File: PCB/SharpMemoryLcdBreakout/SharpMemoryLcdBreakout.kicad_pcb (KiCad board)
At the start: 2 copper layers, 14 x 42 mm, 8 parts, among them J1 Pin Header, J2 EMD, J5 FH12-10S-0.5SH

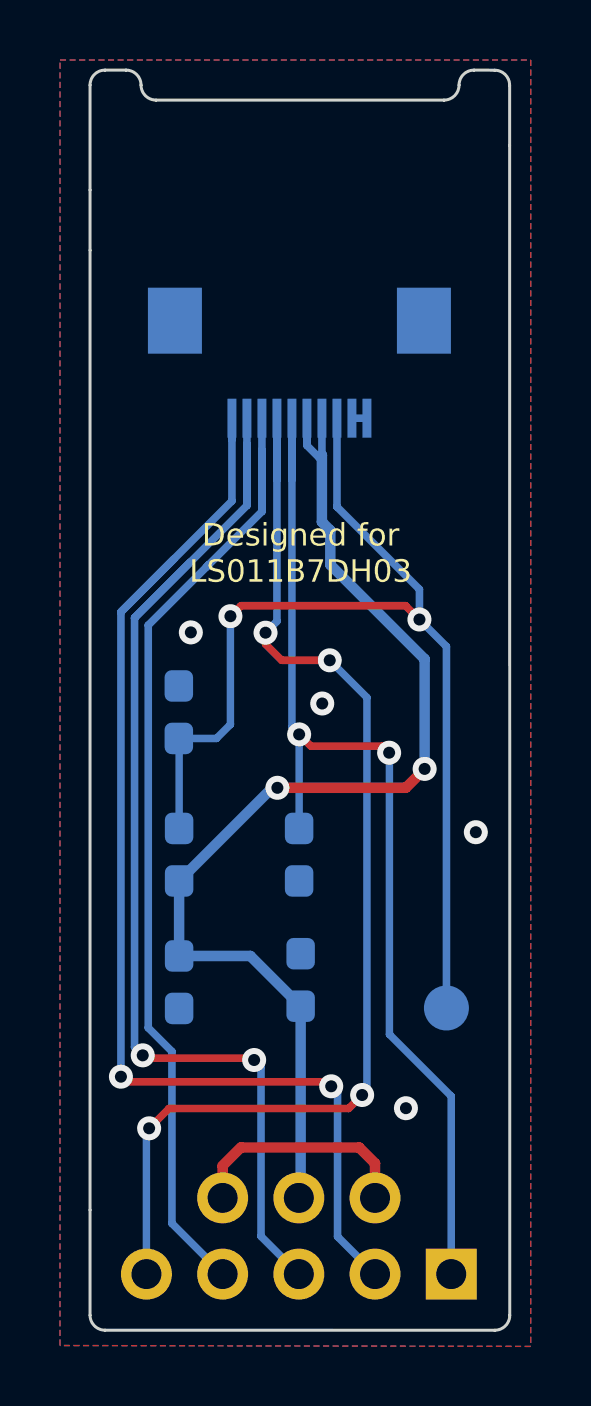
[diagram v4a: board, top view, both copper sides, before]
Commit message: increased part size (0805) and improved silk screen and added ferrite beads
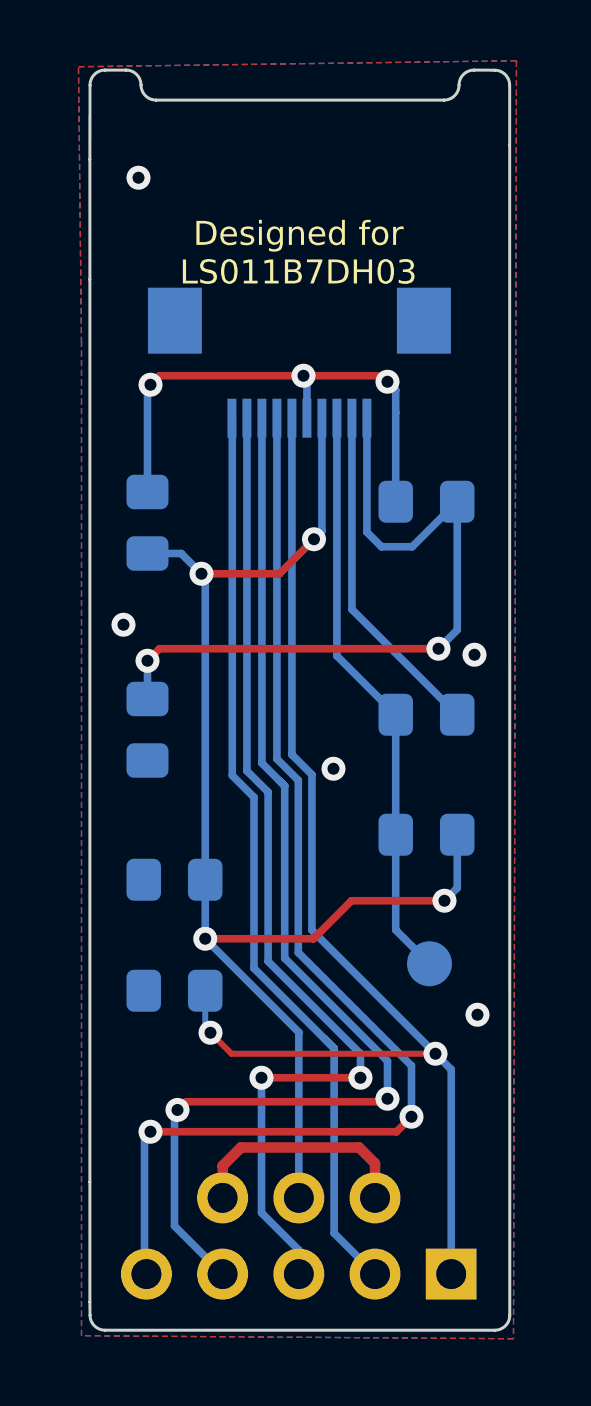
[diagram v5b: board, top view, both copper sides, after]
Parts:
- added FB1: Ferrite_Bead, Resistor_SMD:R_0805_2012Metric_Pad1.15x1.40mm_HandSolder, B.Cu at (104.5, 51.7)
- added FB2: Ferrite_Bead, Resistor_SMD:R_0805_2012Metric_Pad1.15x1.40mm_HandSolder, B.Cu at (104.5, 58.6)
- C1: footprint Capacitor_SMD:C_0603_1608Metric_Pad1.05x0.95mm_HandSolder -> Capacitor_SMD:C_0805_2012Metric_Pad1.15x1.40mm_HandSolder
- C2, C3: value 0.1uF -> 1uF; footprint Capacitor_SMD:C_0603_1608Metric_Pad1.05x0.95mm_HandSolder -> Capacitor_SMD:C_0805_2012Metric_Pad1.15x1.40mm_HandSolder
- R1, R2: footprint Resistor_SMD:R_0603_1608Metric_Pad1.05x0.95mm_HandSolder -> Resistor_SMD:R_0805_2012Metric_Pad1.15x1.40mm_HandSolder
- moved C2 16.5 mm to (113.8, 51.0), turned to 0 degrees
- moved R2 8.27 mm to (113.8, 62.1), turned to 180 degrees
- moved R1 8.26 mm to (113.8, 58.1), turned to 0 degrees
- moved C1 6.15 mm to (105.4, 67.3), turned to 180 degrees
- moved C3 3.42 mm to (105.4, 63.6), turned to 180 degrees
- moved J2 1.58 mm to (113.9, 66.4)
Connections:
- net Net-(C1-Pad1) renamed /DISP
- net Net-(J1-Pad2) renamed /SCLK
- net Net-(J1-Pad3) renamed /SI
- net Net-(J1-Pad4) renamed /SCS
- net Net-(J1-Pad5) renamed /EXTCOMIN
- net Net-(J2-Pad1) renamed /EXTMODE
- C2 pad 1: +3V3 -> VDDA
- C2 pad 2: GND -> GNDA
- J5 pad 10: GND -> GNDA
- J5 pad 6: +3V3 -> VDDA
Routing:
- net GNDA: track 0.00 -> 24.2 mm, vias 0 -> 2
- net VDDA: track 0.00 -> 17.3 mm, vias 0 -> 3
- net /EXTMODE: track 36.5 -> 19.5 mm, vias 2 -> 0
- net GND: track 8.27 -> 19.1 mm, vias 4 -> 5
- net /SCLK: track 40.7 -> 31.0 mm, vias 2 -> 0
- net /SI: track 39.1 -> 33.9 mm
- net +3V3: track 38.8 -> 43.5 mm, vias 2 -> 4
- net /SCS: track 33.3 -> 38.0 mm, vias 0 -> 2
- net /DISP: track 37.3 -> 40.0 mm
- net /EXTCOMIN: track 39.6 -> 39.0 mm, vias 4 -> 2
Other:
- outline, holes or cut-outs redrawn
- board text added: "Sharp Memory LCD Breakout v0.3"
- board text removed: "Sharp Memory LCD Breakout v0.2"

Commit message: Added BOM to readme and updated LCSC parts
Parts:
- C1: value 0.1uF -> 560pF
- renumbered J5 to J3
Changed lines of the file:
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@@
     (property "Sheetname" "")
     (attr smd)
-    (fp_text reference "J5" (at 0.04 -1.4) (layer "B.SilkS")
+    (fp_text reference "J3" (at 0.04 -1.4) (layer "B.SilkS")
       (effects (font (size 0.6 0.6) (thickness 0.1)) (justify mirror))
     )
@@
     (fp_line (start -4.05 1.2) (end -4.05 -3.4) (layer "B.Fab") (width 0.1))
     (pad "1" smd rect (at -2.25 1.85) (locked) (size 0.3 1.3) (layers "B.Cu" "B.Paste" "B.Mask")
-      (net 6 "/SCLK") (pinfunction "Pin_1"))
+      (net 6 "/SCLK") (pinfunction "Pin_1") (pintype "passive"))
     (pad "2" smd rect (at -1.75 1.85) (locked) (size 0.3 1.3) (layers "B.Cu" "B.Paste" "B.Mask")
-      (net 7 "/SI") (pinfunction "Pin_2"))
+      (net 7 "/SI") (pinfunction "Pin_2") (pintype "passive"))
     (pad "3" smd rect (at -1.25 1.85) (locked) (size 0.3 1.3) (layers "B.Cu" "B.Paste" "B.Mask")
-      (net 8 "/SCS") (pinfunction "Pin_3"))
+      (net 8 "/SCS") (pinfunction "Pin_3") (pintype "passive"))
     (pad "4" smd rect (at -0.75 1.85) (locked) (size 0.3 1.3) (layers "B.Cu" "B.Paste" "B.Mask")
-      (net 9 "/EXTCOMIN") (pinfunction "Pin_4"))
+      (net 9 "/EXTCOMIN") (pinfunction "Pin_4") (pintype "passive"))
     (pad "5" smd rect (at -0.25 1.85) (locked) (size 0.3 1.3) (layers "B.Cu" "B.Paste" "B.Mask")
-      (net 2 "/DISP") (pinfunction "Pin_5"))
+      (net 2 "/DISP") (pinfunction "Pin_5") (pintype "passive"))
     (pad "6" smd rect (at 0.25 1.85) (locked) (size 0.3 1.3) (layers "B.Cu" "B.Paste" "B.Mask")
-      (net 4 "VDDA") (pinfunction "Pin_6"))
+      (net 4 "VDDA") (pinfunction "Pin_6") (pintype "passive"))
     (pad "7" smd rect (at 0.75 1.85) (locked) (size 0.3 1.3) (layers "B.Cu" "B.Paste" "B.Mask")
-      (net 3 "+3V3") (pinfunction "Pin_7"))
+      (net 3 "+3V3") (pinfunction "Pin_7") (pintype "passive"))
     (pad "8" smd rect (at 1.25 1.85) (locked) (size 0.3 1.3) (layers "B.Cu" "B.Paste" "B.Mask")
-      (net 10 "/EXTMODE") (pinfunction "Pin_8"))
+      (net 10 "/EXTMODE") (pinfunction "Pin_8") (pintype "passive"))
     (pad "9" smd rect (at 1.75 1.85) (locked) (size 0.3 1.3) (layers "B.Cu" "B.Paste" "B.Mask")
-      (net 1 "GND") (pinfunction "Pin_9"))
+      (net 1 "GND") (pinfunction "Pin_9") (pintype "passive"))
     (pad "10" smd rect (at 2.25 1.85) (locked) (size 0.3 1.3) (layers "B.Cu" "B.Paste" "B.Mask")
-      (net 5 "GNDA") (pinfunction "Pin_10"))
+      (net 5 "GNDA") (pinfunction "Pin_10") (pintype "passive"))
     (pad "MP" smd rect (at 4.15 -1.4) (locked) (size 1.8 2.2) (layers "B.Cu" "B.Paste" "B.Mask"))
     (pad "MP" smd rect (at -4.15 -1.4) (locked) (size 1.8 2.2) (layers "B.Cu" "B.Paste" "B.Mask"))
@@
     (fp_circle (center 0 0) (end 1.25 0) (layer "B.CrtYd") (width 0.05) (fill none))
     (pad "1" smd circle (at 0 0 180) (locked) (size 1.5 1.5) (layers "B.Cu" "B.Mask")
-      (net 10 "/EXTMODE") (pinfunction "Pin_1"))
+      (net 10 "/EXTMODE") (pinfunction "Pin_1") (pintype "passive"))
   )
   (footprint "Capacitor_SMD:C_0805_2012Metric_Pad1.15x1.40mm_HandSolder" (layer "B.Cu")
@@
     (descr "Capacitor SMD 0805 (2012 Metric), square (rectangular) end terminal, IPC_7351 nominal with elongated pad for handsoldering. (Body size source: https://docs.google.com/spreadsheets/d/1BsfQQcO9C6DZCsRaXUlFlo91Tg2WpOkGARC1WS5S8t0/edit?usp=sharing), generated with kicad-footprint-generator")
     (tags "capacitor handsolder")
-    (property "LCSC" "C14663")
+    (property "LCSC" "C28323")
     (property "Sheetfile" "SharpMemoryLcdBreakout.kicad_sch")
     (property "Sheetname" "")
@@
     (descr "Resistor SMD 0805 (2012 Metric), square (rectangular) end terminal, IPC_7351 nominal with elongated pad for handsoldering. (Body size source: https://docs.google.com/spreadsheets/d/1BsfQQcO9C6DZCsRaXUlFlo91Tg2WpOkGARC1WS5S8t0/edit?usp=sharing), generated with kicad-footprint-generator")
     (tags "resistor handsolder")
-    (property "LCSC" "C25804")
+    (property "LCSC" "C365230")
     (property "Sheetfile" "SharpMemoryLcdBreakout.kicad_sch")
     (property "Sheetname" "")
@@
     (descr "Capacitor SMD 0805 (2012 Metric), square (rectangular) end terminal, IPC_7351 nominal with elongated pad for handsoldering. (Body size source: https://docs.google.com/spreadsheets/d/1BsfQQcO9C6DZCsRaXUlFlo91Tg2WpOkGARC1WS5S8t0/edit?usp=sharing), generated with kicad-footprint-generator")
     (tags "capacitor handsolder")
-    (property "LCSC" "C14663")
+    (property "LCSC" "C107119")
     (property "Sheetfile" "SharpMemoryLcdBreakout.kicad_sch")
     (property "Sheetname" "")
@@
       (effects (font (size 1 1) (thickness 0.15)) (justify mirror))
     )
-    (fp_text value "0.1uF" (at 0 -1.65) (layer "B.Fab")
+    (fp_text value "560pF" (at 0 -1.65) (layer "B.Fab")
       (effects (font (size 1 1) (thickness 0.15)) (justify mirror))
     )
@@
     (descr "Resistor SMD 0805 (2012 Metric), square (rectangular) end terminal, IPC_7351 nominal with elongated pad for handsoldering. (Body size source: https://docs.google.com/spreadsheets/d/1BsfQQcO9C6DZCsRaXUlFlo91Tg2WpOkGARC1WS5S8t0/edit?usp=sharing), generated with kicad-footprint-generator")
     (tags "resistor handsolder")
+    (property "LCSC" "C1017")
     (property "Sheetfile" "SharpMemoryLcdBreakout.kicad_sch")
     (property "Sheetname" "")
@@
     (descr "Resistor SMD 0805 (2012 Metric), square (rectangular) end terminal, IPC_7351 nominal with elongated pad for handsoldering. (Body size source: https://docs.google.com/spreadsheets/d/1BsfQQcO9C6DZCsRaXUlFlo91Tg2WpOkGARC1WS5S8t0/edit?usp=sharing), generated with kicad-footprint-generator")
     (tags "resistor handsolder")
-    (property "LCSC" "C25804")
+    (property "LCSC" "C365230")
     (property "Sheetfile" "SharpMemoryLcdBreakout.kicad_sch")
     (property "Sheetname" "")
@@
     (descr "Capacitor SMD 0805 (2012 Metric), square (rectangular) end terminal, IPC_7351 nominal with elongated pad for handsoldering. (Body size source: https://docs.google.com/spreadsheets/d/1BsfQQcO9C6DZCsRaXUlFlo91Tg2WpOkGARC1WS5S8t0/edit?usp=sharing), generated with kicad-footprint-generator")
     (tags "capacitor handsolder")
-    (property "LCSC" "C14663")
+    (property "LCSC" "C28323")
     (property "Sheetfile" "SharpMemoryLcdBreakout.kicad_sch")
     (property "Sheetname" "")
@@
     (descr "Resistor SMD 0805 (2012 Metric), square (rectangular) end terminal, IPC_7351 nominal with elongated pad for handsoldering. (Body size source: https://docs.google.com/spreadsheets/d/1BsfQQcO9C6DZCsRaXUlFlo91Tg2WpOkGARC1WS5S8t0/edit?usp=sharing), generated with kicad-footprint-generator")
     (tags "resistor handsolder")
-    (property "Sheetfile" "SharpMemoryLcdBreakout.kicad_sch")
-    (property "Sheetname" "")
+    (property "LCSC" "C1017")
+    (property "Sheetfile" "SharpMemoryLcdBreakout.kicad_sch")
+    (property "Sheetname" "")

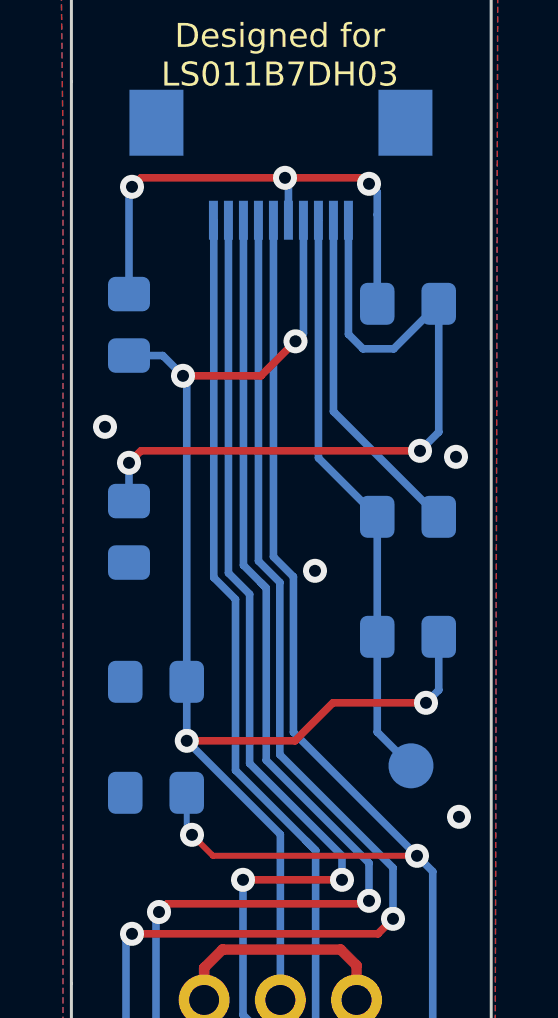
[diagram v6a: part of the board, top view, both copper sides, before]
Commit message: going back to 0603 for easier part selection
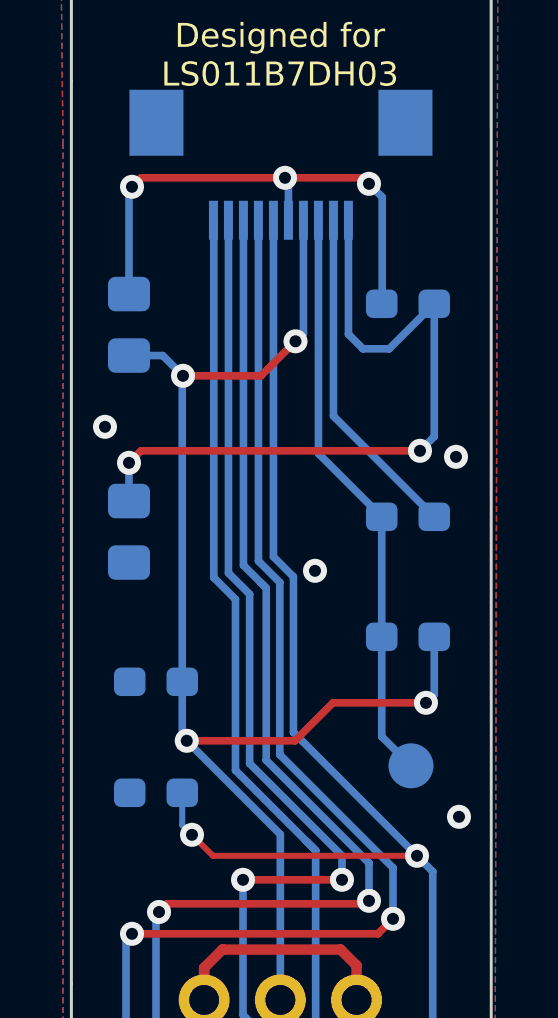
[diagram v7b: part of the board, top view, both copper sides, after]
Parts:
- C1: value 560pF -> 560pF/680pF; footprint Capacitor_SMD:C_0805_2012Metric_Pad1.15x1.40mm_HandSolder -> Capacitor_SMD:C_0603_1608Metric_Pad1.05x0.95mm_HandSolder
- C2, C3: footprint Capacitor_SMD:C_0805_2012Metric_Pad1.15x1.40mm_HandSolder -> Capacitor_SMD:C_0603_1608Metric_Pad1.05x0.95mm_HandSolder
- R1, R2: footprint Resistor_SMD:R_0805_2012Metric_Pad1.15x1.40mm_HandSolder -> Resistor_SMD:R_0603_1608Metric_Pad1.05x0.95mm_HandSolder
